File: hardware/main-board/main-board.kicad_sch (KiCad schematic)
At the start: 98 parts, among them J1 USB_C_Receptacle_USB2.0, J2 DNI, J3 Display Connector, J4 Conn_01x04, SW1 SW_Push, SW2 SW_Push, SW3 SW_Push, SW4 SW_Push, SW5 SW_Detect, SW6 SW_Boot, U1 TSL2585, U2 STM32L072KZT6, U3 MIC4811, U4 USBLC6-2SC6, U5 TC1301A-APA, U6 MIC4811, U7 MCP9808, U8 MIC4811

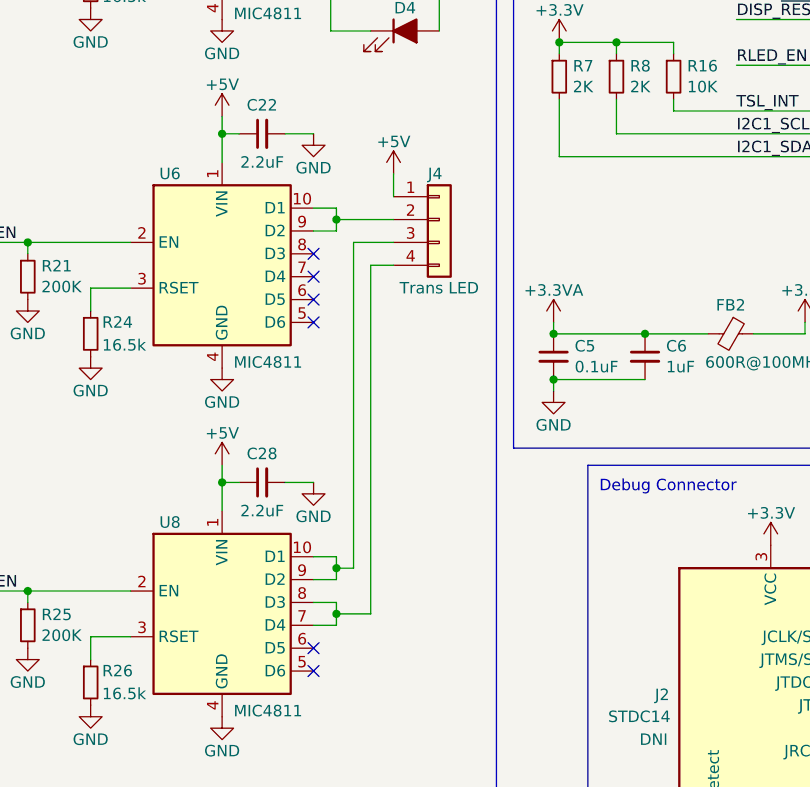
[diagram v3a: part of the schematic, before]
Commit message: Finished first pass at layout for new design changes
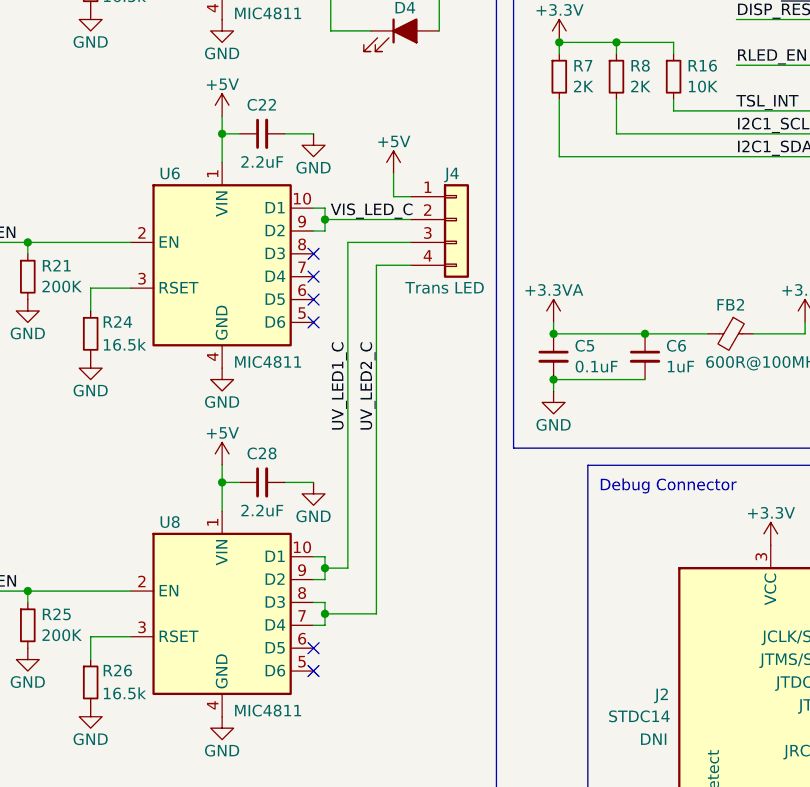
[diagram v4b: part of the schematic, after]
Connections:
- net VIS_LED_C: now reaches J4.2 (Pin_2), U6.10 (D1), U6.9 (D2)
- net UV_LED1_C: now reaches J4.3 (Pin_3), U8.10 (D1), U8.9 (D2)
- net UV_LED2_C: now reaches J4.4 (Pin_4), U8.7 (D4), U8.8 (D3)
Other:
- moved on the sheet: J4
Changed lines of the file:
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@@
   (junction (at 302.26 55.88) (diameter 0) (color 0 0 0 0)
   )
-  (junction (at 109.22 69.85) (diameter 0) (color 0 0 0 0)
+  (junction (at 107.95 69.85) (diameter 0) (color 0 0 0 0)
   )
   (junction (at 214.63 45.72) (diameter 0) (color 0 0 0 0)
@@
   (junction (at 294.005 73.66) (diameter 0) (color 0 0 0 0)
   )
-  (junction (at 109.22 113.665) (diameter 0) (color 0 0 0 0)
+  (junction (at 107.95 113.665) (diameter 0) (color 0 0 0 0)
   )
   (junction (at 253.365 53.34) (diameter 0) (color 0 0 0 0)
@@
   (junction (at 46.99 156.21) (diameter 0) (color 0 0 0 0)
   )
-  (junction (at 109.22 108.585) (diameter 0) (color 0 0 0 0)
+  (junction (at 107.95 108.585) (diameter 0) (color 0 0 0 0)
   )
   (junction (at 146.05 161.925) (diameter 0) (color 0 0 0 0)
@@
     (stroke (width 0) (type default))
   )
-  (wire (pts (xy 106.68 68.58) (xy 109.22 68.58))
+  (wire (pts (xy 106.68 68.58) (xy 107.95 68.58))
     (stroke (width 0) (type default))
   )
@@
     (stroke (width 0) (type default))
   )
-  (wire (pts (xy 109.22 114.935) (xy 106.68 114.935))
+  (wire (pts (xy 107.95 114.935) (xy 106.68 114.935))
     (stroke (width 0) (type default))
   )
@@
     (stroke (width 0) (type default))
   )
-  (wire (pts (xy 106.68 71.12) (xy 109.22 71.12))
+  (wire (pts (xy 106.68 71.12) (xy 107.95 71.12))
     (stroke (width 0) (type default))
   )
@@
     (stroke (width 0) (type default))
   )
-  (wire (pts (xy 109.22 108.585) (xy 109.22 109.855))
+  (wire (pts (xy 107.95 108.585) (xy 107.95 109.855))
+    (stroke (width 0) (type default))
+  )
+  (wire (pts (xy 115.57 67.31) (xy 115.57 64.77))
     (stroke (width 0) (type default))
   )
@@
     (stroke (width 0) (type default))
   )
-  (wire (pts (xy 109.22 109.855) (xy 106.68 109.855))
+  (wire (pts (xy 107.95 109.855) (xy 106.68 109.855))
     (stroke (width 0) (type default))
   )
@@
     (stroke (width 0) (type default))
   )
-  (wire (pts (xy 111.125 108.585) (xy 111.125 72.39))
+  (wire (pts (xy 110.49 108.585) (xy 110.49 72.39))
     (stroke (width 0) (type default))
   )
@@
     (stroke (width 0) (type default))
   )
-  (wire (pts (xy 109.22 112.395) (xy 109.22 113.665))
+  (wire (pts (xy 107.95 112.395) (xy 107.95 113.665))
     (stroke (width 0) (type default))
   )
@@
     (stroke (width 0) (type default))
   )
-  (wire (pts (xy 106.68 112.395) (xy 109.22 112.395))
+  (wire (pts (xy 106.68 112.395) (xy 107.95 112.395))
     (stroke (width 0) (type default))
   )
@@
     (stroke (width 0) (type default))
   )
-  (wire (pts (xy 109.22 107.315) (xy 109.22 108.585))
+  (wire (pts (xy 107.95 107.315) (xy 107.95 108.585))
     (stroke (width 0) (type default))
   )
@@
     (stroke (width 0) (type default))
   )
-  (wire (pts (xy 109.22 69.85) (xy 115.57 69.85))
+  (wire (pts (xy 107.95 69.85) (xy 117.475 69.85))
     (stroke (width 0) (type default))
   )
@@
     (stroke (width 0) (type default))
   )
-  (wire (pts (xy 109.22 113.665) (xy 113.03 113.665))
+  (wire (pts (xy 107.95 113.665) (xy 113.665 113.665))
     (stroke (width 0) (type default))
   )
@@
     (stroke (width 0) (type default))
   )
-  (wire (pts (xy 111.125 72.39) (xy 115.57 72.39))
+  (wire (pts (xy 110.49 72.39) (xy 117.475 72.39))
     (stroke (width 0) (type default))
   )
@@
     (stroke (width 0) (type default))
   )
-  (wire (pts (xy 109.22 69.85) (xy 109.22 71.12))
+  (wire (pts (xy 107.95 69.85) (xy 107.95 71.12))
     (stroke (width 0) (type default))
   )
-  (wire (pts (xy 109.22 108.585) (xy 111.125 108.585))
+  (wire (pts (xy 107.95 108.585) (xy 110.49 108.585))
     (stroke (width 0) (type default))
   )
@@
     (stroke (width 0) (type default))
   )
-  (wire (pts (xy 109.22 68.58) (xy 109.22 69.85))
+  (wire (pts (xy 107.95 68.58) (xy 107.95 69.85))
     (stroke (width 0) (type default))
   )
@@
     (stroke (width 0) (type default))
   )
+  (wire (pts (xy 117.475 67.31) (xy 115.57 67.31))
+    (stroke (width 0) (type default))
+  )
   (wire (pts (xy 108.585 37.465) (xy 106.68 37.465))
     (stroke (width 0) (type default))
@@
     (stroke (width 0) (type default))
   )
-  (wire (pts (xy 113.03 74.93) (xy 115.57 74.93))
+  (wire (pts (xy 113.665 74.93) (xy 117.475 74.93))
     (stroke (width 0) (type default))
   )
@@
     (stroke (width 0) (type default))
   )
-  (wire (pts (xy 113.03 113.665) (xy 113.03 74.93))
+  (wire (pts (xy 113.665 113.665) (xy 113.665 74.93))
     (stroke (width 0) (type default))
   )
@@
     (stroke (width 0) (type default))
   )
-  (wire (pts (xy 109.22 113.665) (xy 109.22 114.935))
+  (wire (pts (xy 107.95 113.665) (xy 107.95 114.935))
     (stroke (width 0) (type default))
   )
@@
     (stroke (width 0) (type default))
   )
-  (wire (pts (xy 115.57 64.77) (xy 115.57 67.31))
-    (stroke (width 0) (type default))
-  )
   (wire (pts (xy 103.505 60.325) (xy 106.68 60.325))
     (stroke (width 0) (type default))
@@
     (stroke (width 0) (type default))
   )
-  (wire (pts (xy 106.68 107.315) (xy 109.22 107.315))
+  (wire (pts (xy 106.68 107.315) (xy 107.95 107.315))
     (stroke (width 0) (type default))
   )
@@
     (effects (font (size 1.27 1.27)) (justify left bottom))
   )
+  (label "UV_LED1_C" (at 110.49 93.345 90) (fields_autoplaced)
+    (effects (font (size 1.27 1.27)) (justify left bottom))
+  )
   (label "BTN4" (at 329.565 81.28 180) (fields_autoplaced)
     (effects (font (size 1.27 1.27)) (justify right bottom))
@@
     (effects (font (size 1.27 1.27)) (justify right bottom))
   )
+  (label "UV_LED2_C" (at 113.665 93.345 90) (fields_autoplaced)
+    (effects (font (size 1.27 1.27)) (justify left bottom))
+  )
   (label "RLED_EN" (at 64.77 33.655 0) (fields_autoplaced)
     (effects (font (size 1.27 1.27)) (justify left bottom))
@@
     (effects (font (size 1.27 1.27)) (justify left bottom))
   )
+  (label "VIS_LED_C" (at 108.585 69.85 0) (fields_autoplaced)
+    (effects (font (size 1.27 1.27)) (justify left bottom))
+  )
   (label "SWDIO" (at 203.2 62.865 180) (fields_autoplaced)
     (effects (font (size 1.27 1.27)) (justify right bottom))
@@
     )
   )
-  (symbol (lib_id "Connector_Generic:Conn_01x04") (at 120.65 69.85 0) (unit 1)
+  (symbol (lib_id "Connector_Generic:Conn_01x04") (at 122.555 69.85 0) (unit 1)
     (in_bom yes) (on_board yes) (dnp no)
-    (property "Reference" "J4" (at 119.38 64.77 0)
+    (property "Reference" "J4" (at 121.285 64.77 0)
       (effects (font (size 1.27 1.27)) (justify left))
     )
-    (property "Value" "Conn_01x04" (at 123.19 72.39 0)
+    (property "Value" "Conn_01x04" (at 125.095 72.39 0)
       (effects (font (size 1.27 1.27)) (justify left) hide)
     )
-    (property "Footprint" "Connector_JST:JST_SH_BM04B-SRSS-TB_1x04-1MP_P1.00mm_Vertical" (at 120.65 69.85 0)
+    (property "Footprint" "Connector_JST:JST_SH_BM04B-SRSS-TB_1x04-1MP_P1.00mm_Vertical" (at 122.555 69.85 0)
       (effects (font (size 1.27 1.27)) hide)
     )
-    (property "Datasheet" "http://www.jst-mfg.com/product/pdf/eng/ePH.pdf" (at 120.65 69.85 0)
+    (property "Datasheet" "http://www.jst-mfg.com/product/pdf/eng/ePH.pdf" (at 122.555 69.85 0)
       (effects (font (size 1.27 1.27)) hide)
     )
-    (property "Description" "CONN HEADER SMD 2POS 1MM" (at 120.65 69.85 0)
+    (property "Description" "CONN HEADER SMD 2POS 1MM" (at 122.555 69.85 0)
       (effects (font (size 1.27 1.27)) hide)
     )
-    (property "Manufacturer" "JST Sales America Inc." (at 120.65 69.85 0)
+    (property "Manufacturer" "JST Sales America Inc." (at 122.555 69.85 0)
       (effects (font (size 1.27 1.27)) hide)
     )
-    (property "Manufacturer PN" "BM04B-SRSS-TB(LF)(SN)" (at 120.65 69.85 0)
+    (property "Manufacturer PN" "BM04B-SRSS-TB(LF)(SN)" (at 122.555 69.85 0)
       (effects (font (size 1.27 1.27)) hide)
     )
-    (property "Supplier" "Digi-Key" (at 120.65 69.85 0)
+    (property "Supplier" "Digi-Key" (at 122.555 69.85 0)
       (effects (font (size 1.27 1.27)) hide)
     )
-    (property "Supplier PN" "455-BM04B-SRSS-TBCT-ND" (at 120.65 69.85 0)
+    (property "Supplier PN" "455-BM04B-SRSS-TBCT-ND" (at 122.555 69.85 0)
       (effects (font (size 1.27 1.27)) hide)
     )
-    (property "User Label" "Trans LED" (at 120.65 77.47 0)
+    (property "User Label" "Trans LED" (at 121.285 77.47 0)
       (effects (font (size 1.27 1.27)))
     )

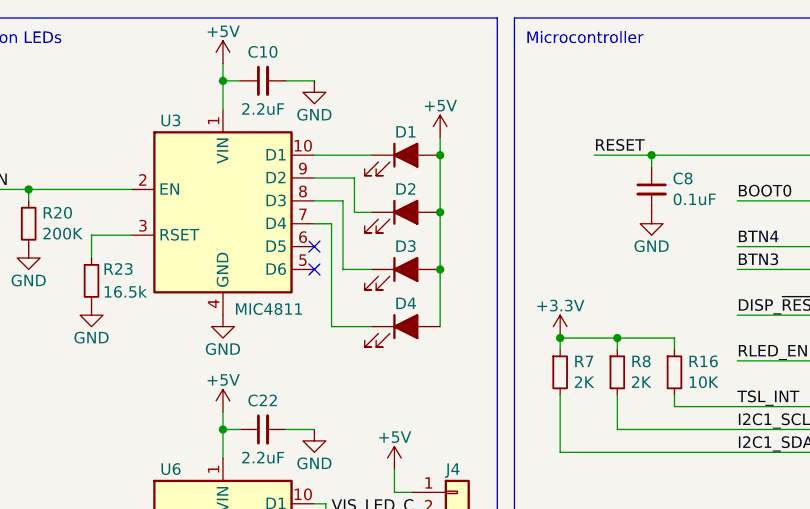
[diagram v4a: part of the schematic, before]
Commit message: Clean up thermal zones around LED footprints
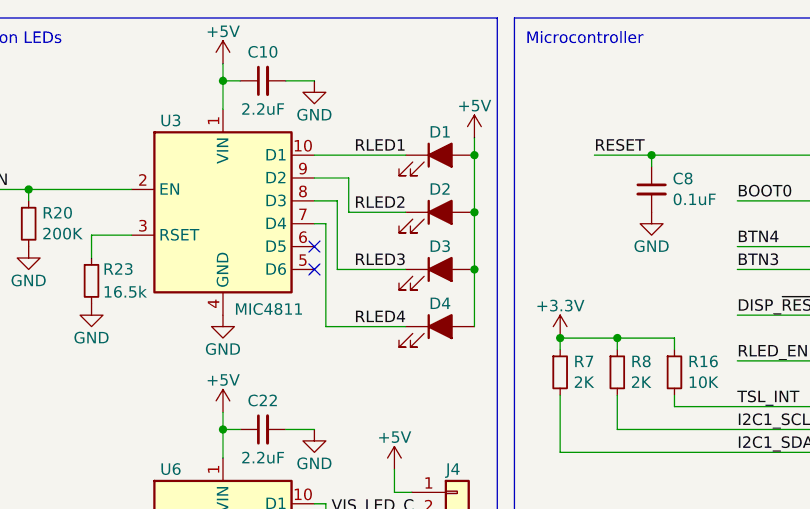
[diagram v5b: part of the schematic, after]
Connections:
- net RLED1: now reaches D1.1 (K), U3.10 (D1)
- net RLED2: now reaches D2.1 (K), U3.9 (D2)
- net RLED3: now reaches D3.1 (K), U3.8 (D3)
- net RLED4: now reaches D4.1 (K), U3.7 (D4)
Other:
- moved on the sheet: D1, D2, D3, D4
